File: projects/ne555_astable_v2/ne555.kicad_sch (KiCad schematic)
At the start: 7 parts, among them U1 NE555

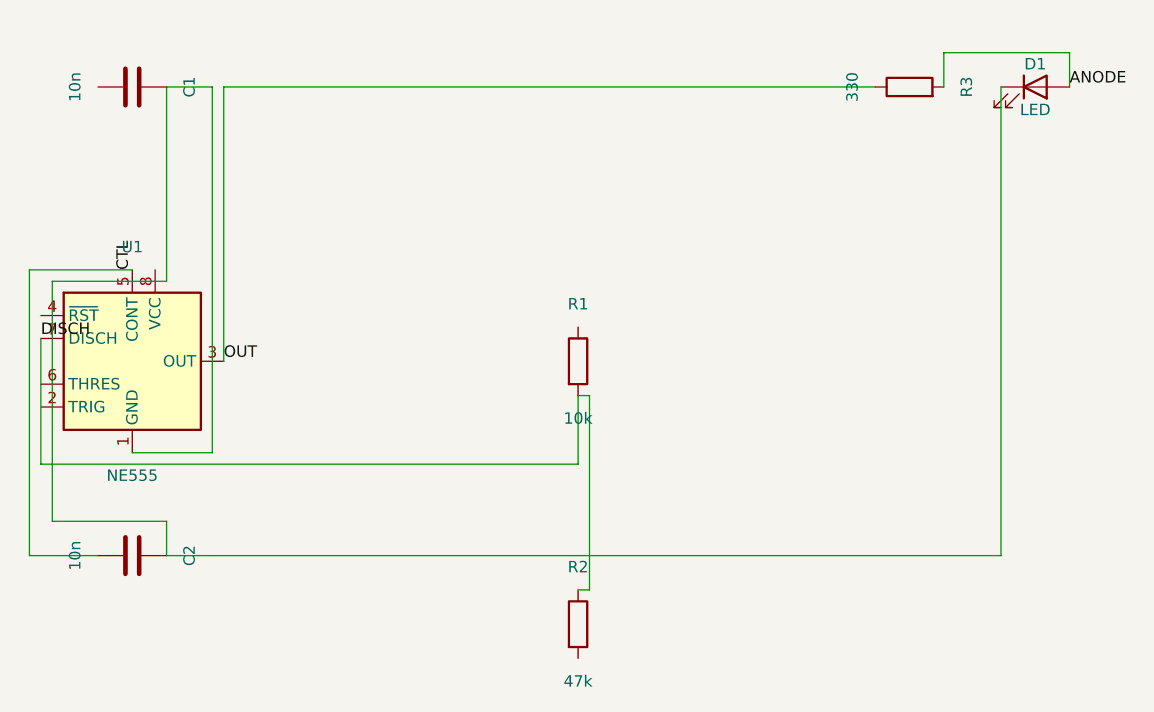
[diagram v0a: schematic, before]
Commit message: Phase 0: KiCad 10 migration + fix blind ERC parsing
- kicad-cli writes JSON reports only to -o file, never stdout; runner
  now uses a temp report file and real JSON decoding
- DetectKicadCLI exported and reused by render_sch and export_test
- KiCad 10 symbol renames (ATmega328-AU -> ATmega328-A) and pin
  numbers fixed in demos

Co-Authored-By: Claude Fable 5 <noreply@anthropic.com>
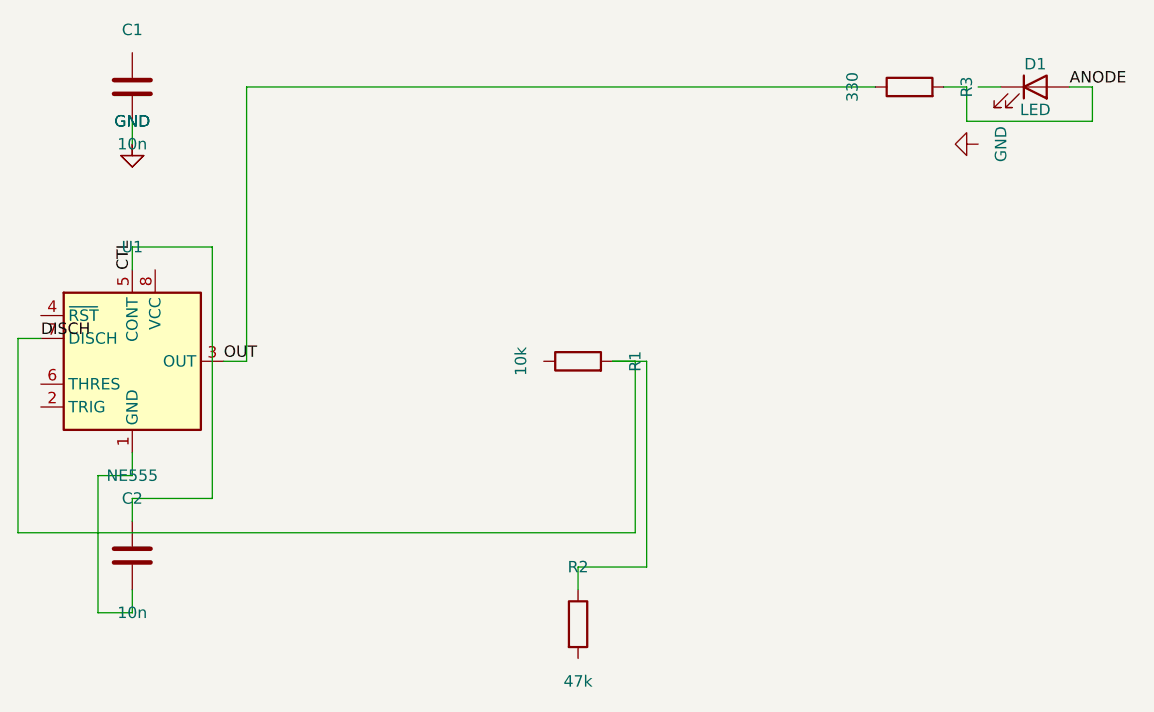
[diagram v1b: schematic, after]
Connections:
- net at C2.2, U1.1 (GND): no longer C1.2, D1.1 (K)
- new net GND: C1.2

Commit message: Phase 1: geometric quality gate (internal/place2/gate)
Post-hoc Enforce() guarantees zero cross-net crossings, zero wires
through symbol bodies, zero collinear overlaps: offending nets are
demoted to net labels (no geometry, identical connectivity). Wired
into connect_netlist and relayout. Same-net duplicate segments are
merged by Clean, not demoted.

Co-Authored-By: Claude Fable 5 <noreply@anthropic.com>
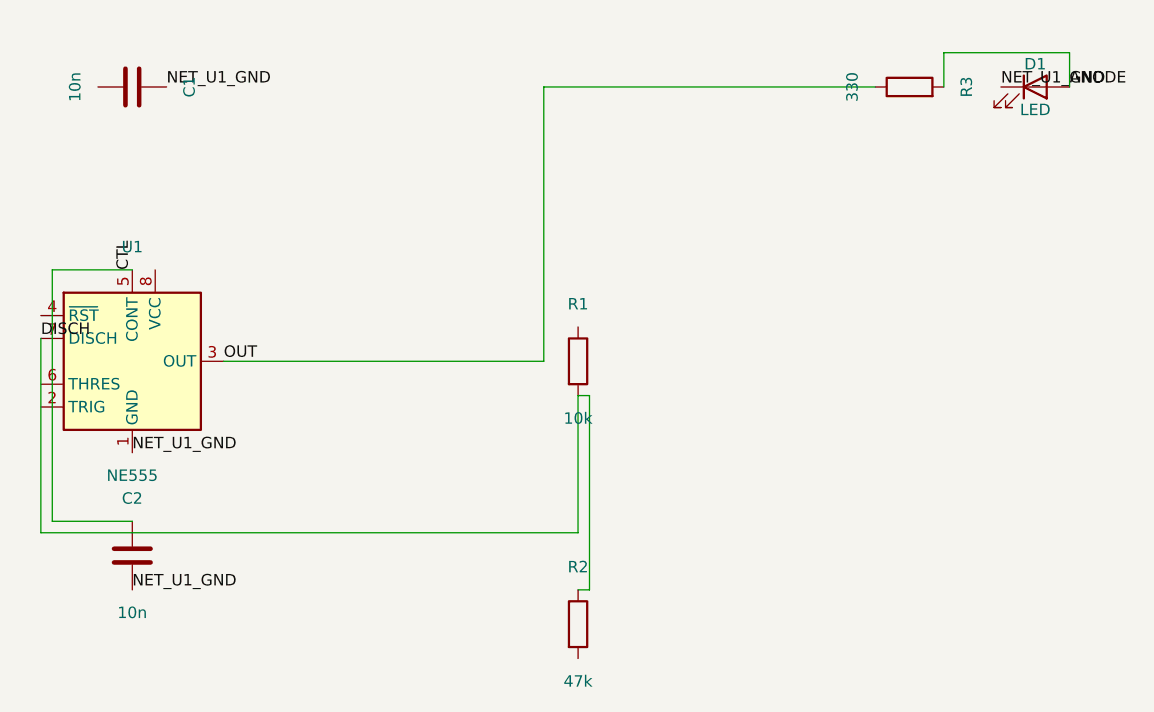
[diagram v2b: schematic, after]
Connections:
- net GND is gone; now on net NET_U1_GND: C1.2
- net NET_U1_GND: now reaches D1.1 (K)
- net NET_U1_GND: now also C2.2, U1.1 (GND)

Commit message: Phase 2: baked template geometry + LM358 embed fix
Templates now carry hand-authored wires/junctions/labels in relative
coords; Stamp() emits them verbatim. All 5 templates rewritten with
human conventions and self-verifying tests (gate.Check==0, TraceNets
contract, exact pin-endpoint match). flattenRawSymbol now inherits
parent properties so embedded derived symbols match KiCad 10
regeneration (fixes lib_symbol_mismatch for LM358/NE5532).

Co-Authored-By: Claude Fable 5 <noreply@anthropic.com>
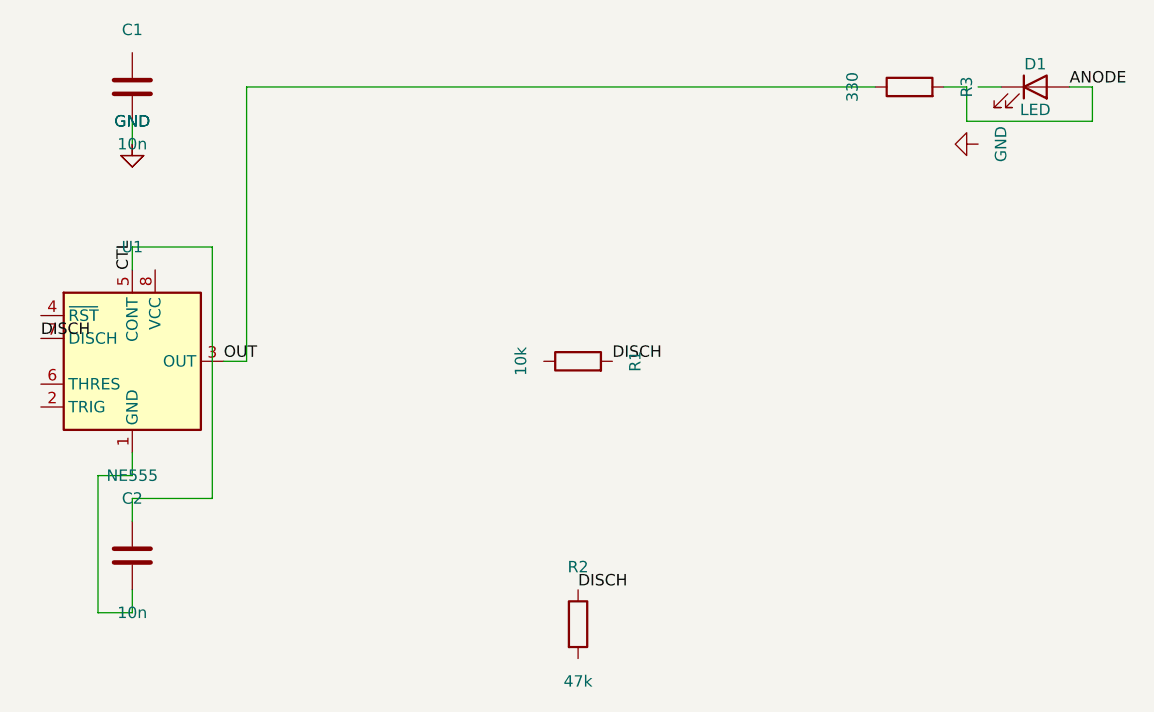
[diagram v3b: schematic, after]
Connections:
- net NET_U1_GND: no longer names the net of C2.2, U1.1 (GND)
- net NET_U1_GND: no longer C1.2, D1.1 (K)
- new net GND: C1.2

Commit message: Phase 3: parametric cluster wiring generators (internal/place2/wiregen)
Closed-form wiring (straight or single-L with clear-corridor
preconditions) for decoupling, 2-pin satellites, dividers and crystal
load caps; generators apply or decline, never search. Integrated as a
pre-pass in connect_netlist with component-aware MST; discovery-label
fallback now also fires for nets fully consumed by wiregen (fixes
dropped-net regression, covered by two regression tests).

Co-Authored-By: Claude Fable 5 <noreply@anthropic.com>
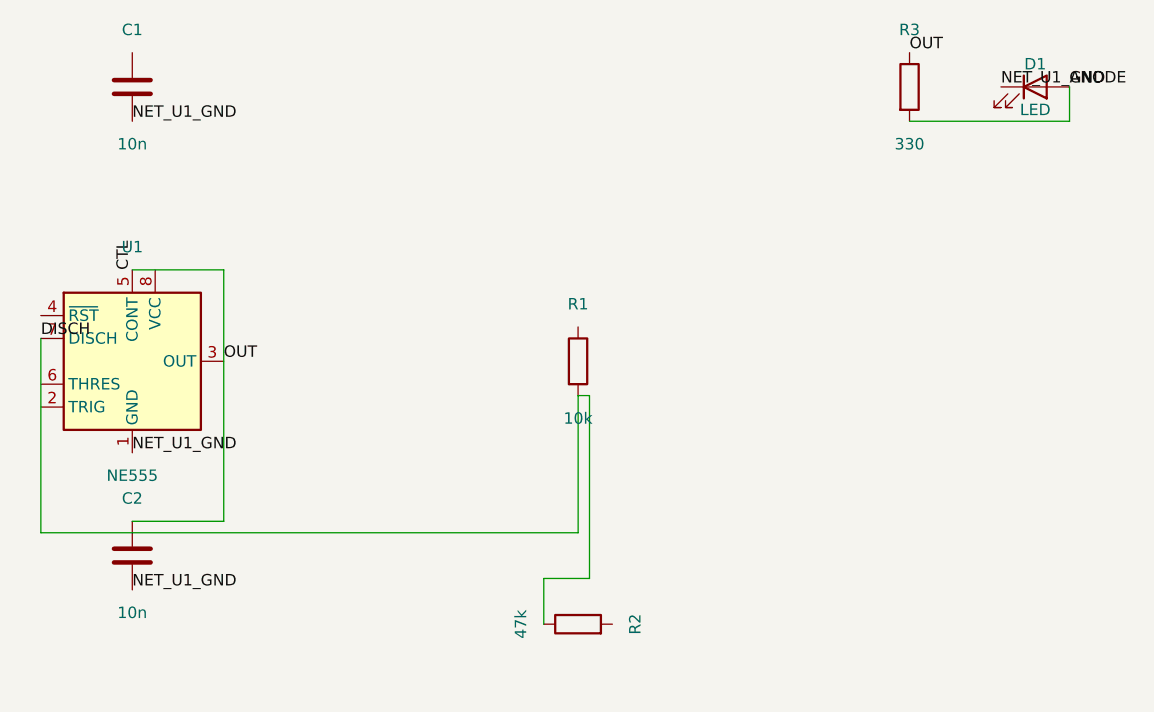
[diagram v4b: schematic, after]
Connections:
- net GND is gone; now on net NET_U1_GND: C1.2
- net OUT is gone; now on net CTL: R3.1, U1.3 (OUT)
- net NET_U1_GND: now reaches D1.1 (K)
- net NET_U1_GND: now also C2.2, U1.1 (GND)

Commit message: Phase 4: per-pin power rail policy + full pipeline determinism
Power nets are never routed: every pin on a rail gets its own power
symbol (GND down, VCC up) with a 2.54mm stub; PWR_FLAG emitted after
the gate for undriven power_in nets. Determinism: cluster detection
and TraceNets no longer depend on Go map iteration order (refOrder
slices, sorted canonical net naming). 6/6 identical runs on vreg and
mcu demos; vreg ERC now has zero errors.

Co-Authored-By: Claude Fable 5 <noreply@anthropic.com>
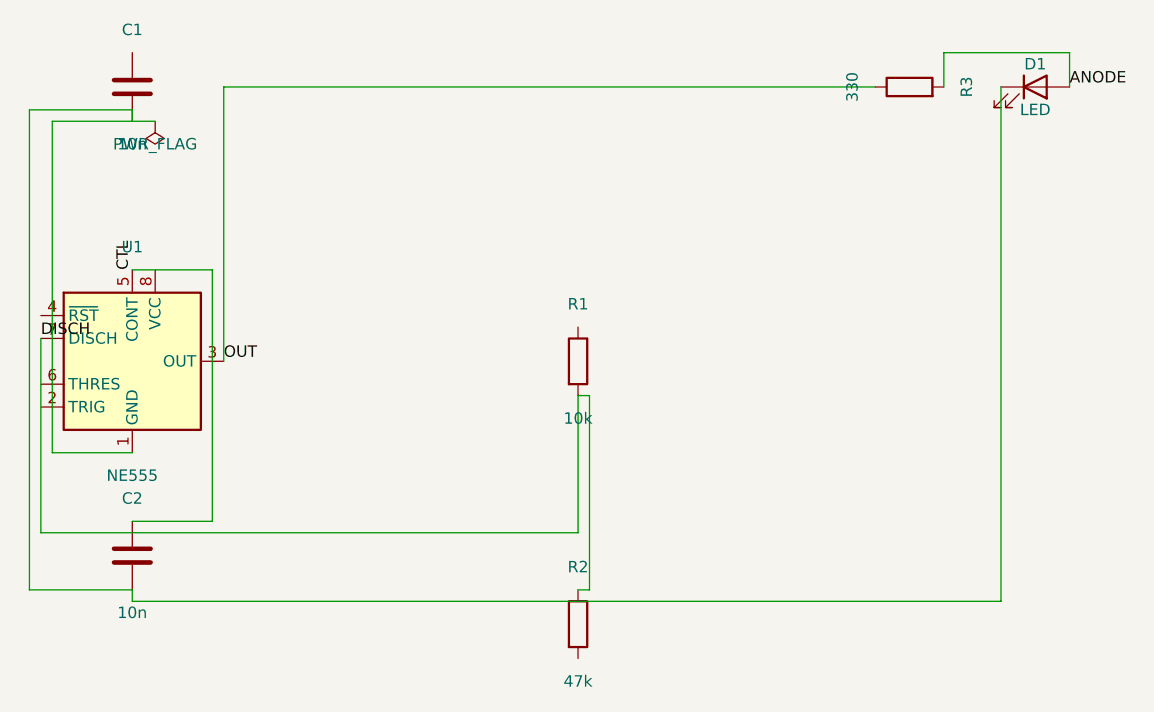
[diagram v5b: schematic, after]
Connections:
- net CTL: no longer R3.1, U1.3 (OUT)
- net NET_U1_GND: no longer names the net of C1.2, C2.2, D1.1 (K), U1.1 (GND)
- new net OUT: R3.1, U1.3 (OUT)
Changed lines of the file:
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@@
     (instances
       (project ""
-        (path "/14731445-e103-4df4-9a3d-e796989cc43f" (reference "U1") (unit 1)))))
+        (path "/8081636c-36a4-4d7f-a29f-77afa4d5e712" (reference "U1") (unit 1)))))
   (symbol (lib_id "Device:R")
     (at 100.33 81.28 0) (unit 1) (exclude_from_sim no) (in_bom yes) (on_board yes) (dnp no)
@@
     (instances
       (project ""
-        (path "/14731445-e103-4df4-9a3d-e796989cc43f" (reference "R1") (unit 1)))))
+        (path "/8081636c-36a4-4d7f-a29f-77afa4d5e712" (reference "R1") (unit 1)))))
   (symbol (lib_id "Device:R")
-    (at 100.33 110.49 90) (unit 1) (exclude_from_sim no) (in_bom yes) (on_board yes) (dnp no)
+    (at 100.33 110.49 0) (unit 1) (exclude_from_sim no) (in_bom yes) (on_board yes) (dnp no)
     (property "Reference" "R2"
-      (at 106.68 110.49 0)
+      (at 100.33 104.14 0)
       (effects
         (font (size 1.27 1.27))))
     (property "Value" "47k"
-      (at 93.98 110.49 0)
+      (at 100.33 116.84 0)
       (effects
         (font (size 1.27 1.27))))
@@
     (instances
       (project ""
-        (path "/14731445-e103-4df4-9a3d-e796989cc43f" (reference "R2") (unit 1)))))
+        (path "/8081636c-36a4-4d7f-a29f-77afa4d5e712" (reference "R2") (unit 1)))))
   (symbol (lib_id "Device:C")
     (at 50.8 50.8 0) (unit 1) (exclude_from_sim no) (in_bom yes) (on_board yes) (dnp no)
@@
     (instances
       (project ""
-        (path "/14731445-e103-4df4-9a3d-e796989cc43f" (reference "C1") (unit 1)))))
+        (path "/8081636c-36a4-4d7f-a29f-77afa4d5e712" (reference "C1") (unit 1)))))
   (symbol (lib_id "Device:C")
     (at 50.8 102.87 0) (unit 1) (exclude_from_sim no) (in_bom yes) (on_board yes) (dnp no)
@@
     (instances
       (project ""
-        (path "/14731445-e103-4df4-9a3d-e796989cc43f" (reference "C2") (unit 1)))))
+        (path "/8081636c-36a4-4d7f-a29f-77afa4d5e712" (reference "C2") (unit 1)))))
   (symbol (lib_id "Device:LED")
     (at 151.13 50.8 0) (unit 1) (exclude_from_sim no) (in_bom yes) (on_board yes) (dnp no)
@@
     (instances
       (project ""
-        (path "/14731445-e103-4df4-9a3d-e796989cc43f" (reference "D1") (unit 1)))))
+        (path "/8081636c-36a4-4d7f-a29f-77afa4d5e712" (reference "D1") (unit 1)))))
   (symbol (lib_id "Device:R")
-    (at 137.16 50.8 0) (unit 1) (exclude_from_sim no) (in_bom yes) (on_board yes) (dnp no)
+    (at 137.16 50.8 90) (unit 1) (exclude_from_sim no) (in_bom yes) (on_board yes) (dnp no)
     (property "Reference" "R3"
-      (at 137.16 44.45 0)
+      (at 143.51 50.8 0)
       (effects
         (font (size 1.27 1.27))))
     (property "Value" "330"
-      (at 137.16 57.15 0)
+      (at 130.81 50.8 0)
       (effects
         (font (size 1.27 1.27))))
@@
     (instances
       (project ""
-        (path "/14731445-e103-4df4-9a3d-e796989cc43f" (reference "R3") (unit 1)))))
+        (path "/8081636c-36a4-4d7f-a29f-77afa4d5e712" (reference "R3") (unit 1)))))
   (label "ANODE"
     (at 154.94 50.8 0) (fields_autoplaced yes)
@@
       (effects
         (font (size 1.27 1.27)) (hide yes))))
-  (wire
-    (pts (xy 154.94 50.8) (xy 154.94 54.61))
-    (stroke (width 0) (type default)))
-  (wire
-    (pts (xy 154.94 54.61) (xy 137.16 54.61))
-    (stroke (width 0) (type default)))
-  (wire
-    (pts (xy 50.8 71.12) (xy 60.96 71.12))
-    (stroke (width 0) (type default)))
-  (wire
-    (pts (xy 60.96 71.12) (xy 60.96 99.06))
-    (stroke (width 0) (type default)))
-  (wire
-    (pts (xy 60.96 99.06) (xy 50.8 99.06))
-    (stroke (width 0) (type default)))
-  (wire
-    (pts (xy 40.64 78.74) (xy 40.64 100.33))
-    (stroke (width 0) (type default)))
-  (wire
-    (pts (xy 40.64 100.33) (xy 100.33 100.33))
-    (stroke (width 0) (type default)))
-  (wire
-    (pts (xy 100.33 100.33) (xy 100.33 85.09))
-    (stroke (width 0) (type default)))
-  (wire
-    (pts (xy 100.33 85.09) (xy 101.6 85.09))
-    (stroke (width 0) (type default)))
-  (wire
-    (pts (xy 101.6 85.09) (xy 101.6 105.41))
-    (stroke (width 0) (type default)))
-  (wire
-    (pts (xy 101.6 105.41) (xy 96.52 105.41))
-    (stroke (width 0) (type default)))
-  (wire
-    (pts (xy 96.52 105.41) (xy 96.52 110.49))
-    (stroke (width 0) (type default)))
-  (label "NET_U1_GND"
-    (at 50.8 91.44 0) (fields_autoplaced yes)
-    (effects
-      (font (size 1.27 1.27)) (justify left bottom))
-    (property "Intersheet References" ""
-      (at 0 0 0)
-      (effects
-        (font (size 1.27 1.27)) (hide yes))))
-  (label "NET_U1_GND"
-    (at 50.8 54.61 0) (fields_autoplaced yes)
-    (effects
-      (font (size 1.27 1.27)) (justify left bottom))
-    (property "Intersheet References" ""
-      (at 0 0 0)
-      (effects
-        (font (size 1.27 1.27)) (hide yes))))
-  (label "NET_U1_GND"
-    (at 50.8 106.68 0) (fields_autoplaced yes)
-    (effects
-      (font (size 1.27 1.27)) (justify left bottom))
-    (property "Intersheet References" ""
-      (at 0 0 0)
-      (effects
-        (font (size 1.27 1.27)) (hide yes))))
-  (label "NET_U1_GND"
-    (at 147.32 50.8 0) (fields_autoplaced yes)
-    (effects
-      (font (size 1.27 1.27)) (justify left bottom))
-    (property "Intersheet References" ""
-      (at 0 0 0)
-      (effects
-        (font (size 1.27 1.27)) (hide yes))))
   (label "OUT"
     (at 60.96 81.28 0) (fields_autoplaced yes)
@@
       (effects
         (font (size 1.27 1.27)) (hide yes))))
-  (label "OUT"
-    (at 137.16 46.99 0) (fields_autoplaced yes)
-    (effects
-      (font (size 1.27 1.27)) (justify left bottom))
-    (property "Intersheet References" ""
-      (at 0 0 0)
-      (effects
-        (font (size 1.27 1.27)) (hide yes)))))
+  (wire
+    (pts (xy 154.94 50.8) (xy 154.94 46.99))
+    (stroke (width 0) (type default)))
+  (wire
+    (pts (xy 154.94 46.99) (xy 140.97 46.99))
+    (stroke (width 0) (type default)))
+  (wire
+    (pts (xy 140.97 46.99) (xy 140.97 50.8))
+    (stroke (width 0) (type default)))
+  (wire
+    (pts (xy 50.8 71.12) (xy 59.69 71.12))
+    (stroke (width 0) (type default)))
+  (wire
+    (pts (xy 59.69 71.12) (xy 59.69 99.06))
+    (stroke (width 0) (type default)))
+  (wire
+    (pts (xy 59.69 99.06) (xy 50.8 99.06))
+    (stroke (width 0) (type default)))
+  (wire
+    (pts (xy 40.64 78.74) (xy 40.64 100.33))
+    (stroke (width 0) (type default)))
+  (wire
+    (pts (xy 40.64 100.33) (xy 100.33 100.33))
+    (stroke (width 0) (type default)))
+  (wire
+    (pts (xy 100.33 100.33) (xy 100.33 85.09))
+    (stroke (width 0) (type default)))
+  (wire
+    (pts (xy 100.33 85.09) (xy 101.6 85.09))
+    (stroke (width 0) (type default)))
+  (wire
+    (pts (xy 101.6 85.09) (xy 101.6 106.68))
+    (stroke (width 0) (type default)))
+  (wire
+    (pts (xy 101.6 106.68) (xy 100.33 106.68))
+    (stroke (width 0) (type default)))
+  (wire
+    (pts (xy 50.8 91.44) (xy 41.91 91.44))
+    (stroke (width 0) (type default)))
+  (wire
+    (pts (xy 41.91 91.44) (xy 41.91 54.61))
+    (stroke (width 0) (type default)))
+  (wire
+    (pts (xy 41.91 54.61) (xy 50.8 54.61))
+    (stroke (width 0) (type default)))
+  (wire
+    (pts (xy 50.8 54.61) (xy 50.8 53.34))
+    (stroke (width 0) (type default)))
+  (wire
+    (pts (xy 50.8 53.34) (xy 39.37 53.34))
+    (stroke (width 0) (type default)))
+  (wire
+    (pts (xy 39.37 53.34) (xy 39.37 106.68))
+    (stroke (width 0) (type default)))
+  (wire
+    (pts (xy 39.37 106.68) (xy 50.8 106.68))
+    (stroke (width 0) (type default)))
+  (wire
+    (pts (xy 50.8 106.68) (xy 50.8 107.95))
+    (stroke (width 0) (type default)))
+  (wire
+    (pts (xy 50.8 107.95) (xy 147.32 107.95))
+    (stroke (width 0) (type default)))
+  (wire
+    (pts (xy 147.32 107.95) (xy 147.32 50.8))
+    (stroke (width 0) (type default)))
+  (wire
+    (pts (xy 60.96 81.28) (xy 60.96 50.8))
+    (stroke (width 0) (type default)))
+  (wire
+    (pts (xy 60.96 50.8) (xy 133.35 50.8))
+    (stroke (width 0) (type default)))
+  (symbol (lib_id "power:PWR_FLAG")
+    (at 53.34 54.61 180) (unit 1) (exclude_from_sim no) (in_bom no) (on_board no) (dnp no)
+    (property "Reference" "#FLG01"
+      (at 53.34 54.61 0)
+      (effects
+        (font (size 1.27 1.27)) (hide yes)))
+    (property "Value" "PWR_FLAG"
+      (at 53.34 57.15 0)
+      (effects
+        (font (size 1.27 1.27))))
+    (property "Footprint" ""
+      (at 53.34 54.61 0)
+      (effects
+        (font (size 1.27 1.27)) (hide yes)))
+    (property "Datasheet" ""
+      (at 53.34 54.61 0)
+      (effects
+        (font (size 1.27 1.27)) (hide yes)))
+    (property "Description" ""
+      (at 53.34 54.61 0)
+      (effects
+        (font (size 1.27 1.27)) (hide yes)))
+    (pin "1")
+    (instances
+      (project ""
+        (path "/8081636c-36a4-4d7f-a29f-77afa4d5e712" (reference "#FLG01") (unit 1)))))
+  (wire
+    (pts (xy 50.8 54.61) (xy 53.34 54.61))
+    (stroke (width 0) (type default))))
